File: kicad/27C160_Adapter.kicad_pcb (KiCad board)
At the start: 2 copper layers, 82.4 x 43.1 mm, 10 parts, among them Q1 BC327, SW1 MS22D16, SW2 DIP, U1 27C4002

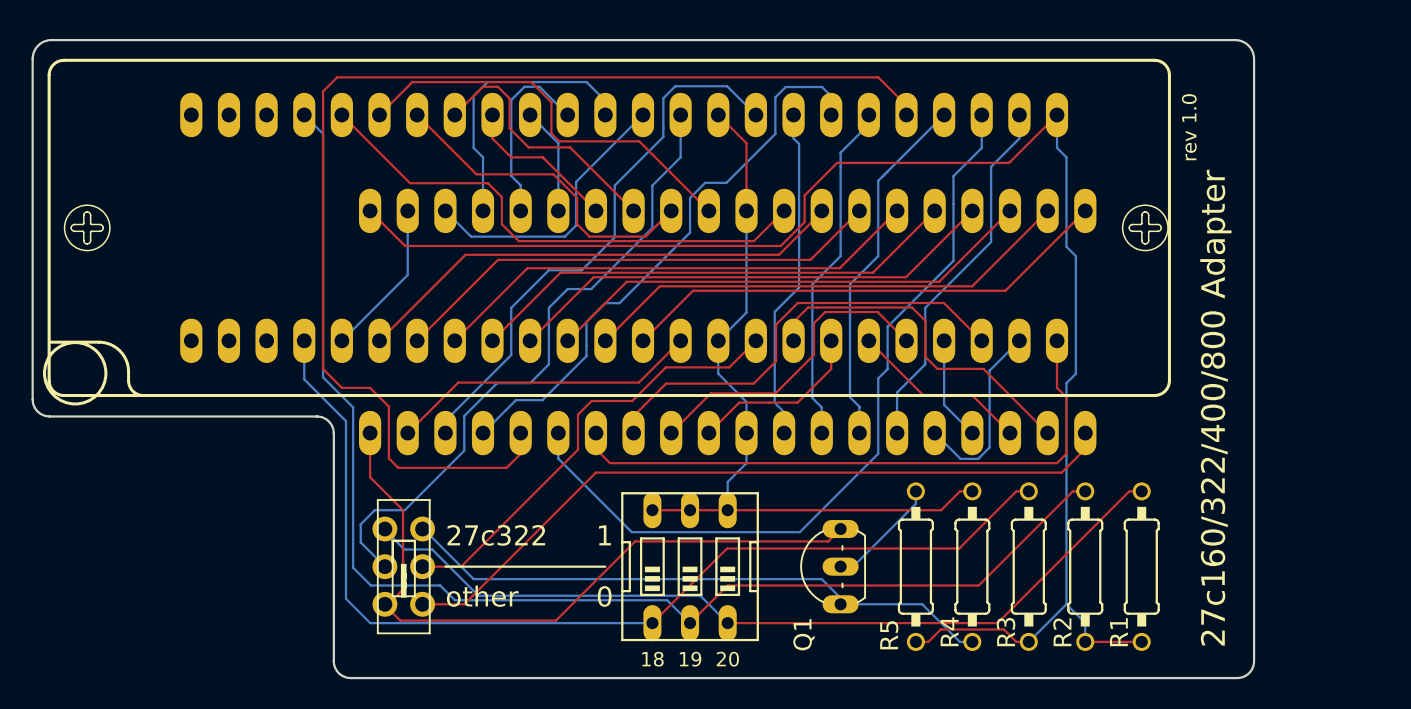
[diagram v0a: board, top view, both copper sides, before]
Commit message: Shrunk PCB size Converted resistors and transistor to SMD Introduced GND fills Converted to Kicad 5.x
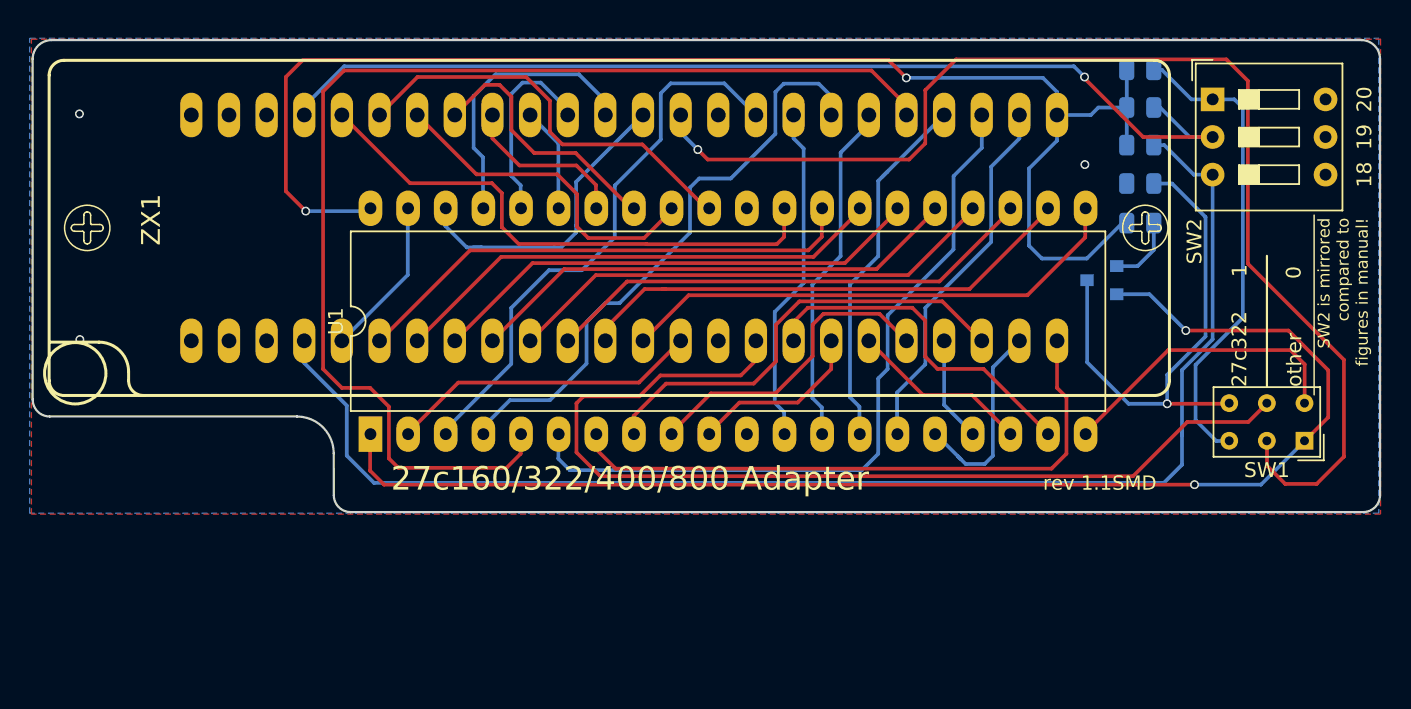
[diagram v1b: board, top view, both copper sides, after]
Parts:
- Q1: value BC327 -> BC807; footprint TO92-EBC -> Package_TO_SOT_SMD:SOT-23; moved to B.Cu
- R1, R2, R3, R4, R5: footprint 0207%2f10 -> Resistor_SMD:R_0805_2012Metric; moved to B.Cu
- SW1: footprint MS22D16 -> Button_Switch_THT:SW_NKK_GW12LJP
- SW2: footprint EDG-03 -> Button_Switch_THT:SW_DIP_SPSTx03_Slide_9.78x9.8mm_W7.62mm_P2.54mm
- U1: footprint 27C4002 -> Package_DIP:DIP-40_W15.24mm_LongPads
- ZX1: footprint 3M_248-3345 -> 27C160_Adapter:3M_248-3345
- moved SW1 61.4 mm to (193.1, 110.5), turned to 180 degrees
- moved SW2 47.3 mm to (186.9, 87.4)
- moved R1 33.5 mm to (182.1, 85.4), turned to 180 degrees
- moved R2 31.2 mm to (182.1, 88.0), turned to 180 degrees
- moved R3 29.4 mm to (182.1, 90.5), turned to 180 degrees
- moved R4 28.2 mm to (182.1, 93.1), turned to 0 degrees
- moved R5 27.7 mm to (182.1, 95.8), turned to 0 degrees
- moved Q1 27.0 mm to (179.5, 99.6), turned to 180 degrees
- moved U1 24.1 mm to (130.1, 110.0), turned to 90 degrees
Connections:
- SW2 pad 1: /A18 -> /A20
- SW2 pad 3: /A20 -> /A18
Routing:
- net GND: track 51.7 -> 0.00 mm, vias 0 -> 3
- net /VPP: track 46.9 -> 89.0 mm, vias 0 -> 2
- net /N$2: track 43.5 -> 81.9 mm, vias 0 -> 1
- net /N$6: track 30.2 -> 67.2 mm
- net /N$5: track 50.1 -> 20.2 mm
- net /A20: track 57.5 -> 32.3 mm
- net /A18: track 69.0 -> 92.0 mm
- net /A19: track 86.6 -> 69.8 mm, vias 0 -> 1
- net VCC: track 104.6 -> 96.4 mm, vias 0 -> 2
- net /N$4: track 40.5 -> 34.4 mm, vias 0 -> 1
- net /D12: track 53.3 -> 49.9 mm
- net /N$1: track 7.68 -> 4.76 mm
- net /A16: track 19.2 -> 21.2 mm
- net /A8: track 35.3 -> 36.8 mm
- net /D14: track 38.8 -> 40.2 mm
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- added copper zone on B.Cu, net GND
- added copper zone on F.Cu, net GND
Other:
- board size 82.4 x 43.1 mm -> 90.9 x 31.9 mm
- board text added: "R1-5: 10kOhm Q1: BC807"
- board text added: "SMD Variant by torsti76 <amiga@tk-webart.de>"
- board text added: "SW2 is mirrored compared to figures in manual!"
- board text added: "rev 1.1SMD"
- board text removed: "R1-5: 10kOhm Q1: BC327"
- board text removed: "rev 1.0"

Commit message: Refinements / Upgrade to KiCAD 6
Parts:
- SW1: footprint Button_Switch_THT:SW_NKK_GW12LJP -> 27C160_Adapter:MS22D16
- U1: footprint Package_DIP:DIP-40_W15.24mm_LongPads -> 27C160_Adapter:27C4002
- moved U1 24.1 mm to (153.0, 102.5), turned to 0 degrees
- moved SW1 2.84 mm to (190.6, 109.2)
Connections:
- ZX1 pad 1: (no net) -> unconnected-(ZX1-Pad1)
- ZX1 pad 2: (no net) -> unconnected-(ZX1-Pad2)
- ZX1 pad 3: (no net) -> unconnected-(ZX1-Pad3)
- ZX1 pad 46: (no net) -> unconnected-(ZX1-Pad46)
- ZX1 pad 47: (no net) -> unconnected-(ZX1-Pad47)
- ZX1 pad 48: (no net) -> unconnected-(ZX1-Pad48)
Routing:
- net /A16: track 21.2 -> 20.7 mm
- net GND: vias 3 -> 6
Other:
- net class Default removed
- board text removed: "SW2 is mirrored compared to figures in manual!"
